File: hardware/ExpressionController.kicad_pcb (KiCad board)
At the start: 2 copper layers, 84.8 x 61.5 mm, 132 parts, among them J1 DC, J2 Exp1, J3 Exp2, J4 Exp3, J5 Exp4, Q1 DMP3099L-7, U1 ADP7142AUJZ-3.3, U10 74HC595, U11 SN74LVC126A, U12 74HC595, U13 SN74LVC126A, U14 74AHCT1G125, U2 ADP7142AUJZ-5.0, U3 ADP7142AUJZ-2.5, U4 AD7718, U5 AD7718, U6 74HC595, U7 SN74LVC126A, U8 74HC595, U9 SN74LVC126A, Y1 MS1V-T1K-32.768kHz-12.5pF-20P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, Y2 MS1V-T1K-32.768kHz-12.5pF-20P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

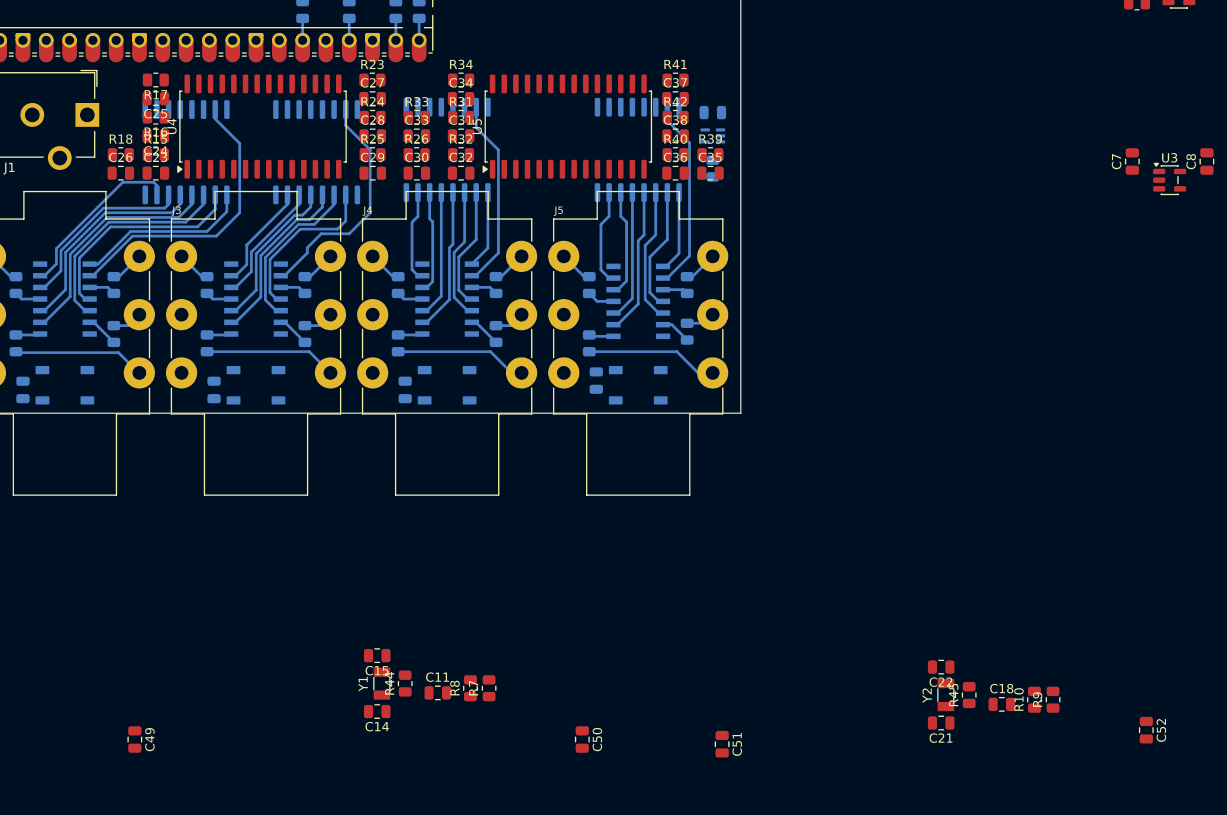
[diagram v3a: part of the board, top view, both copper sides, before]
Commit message: more routing changes
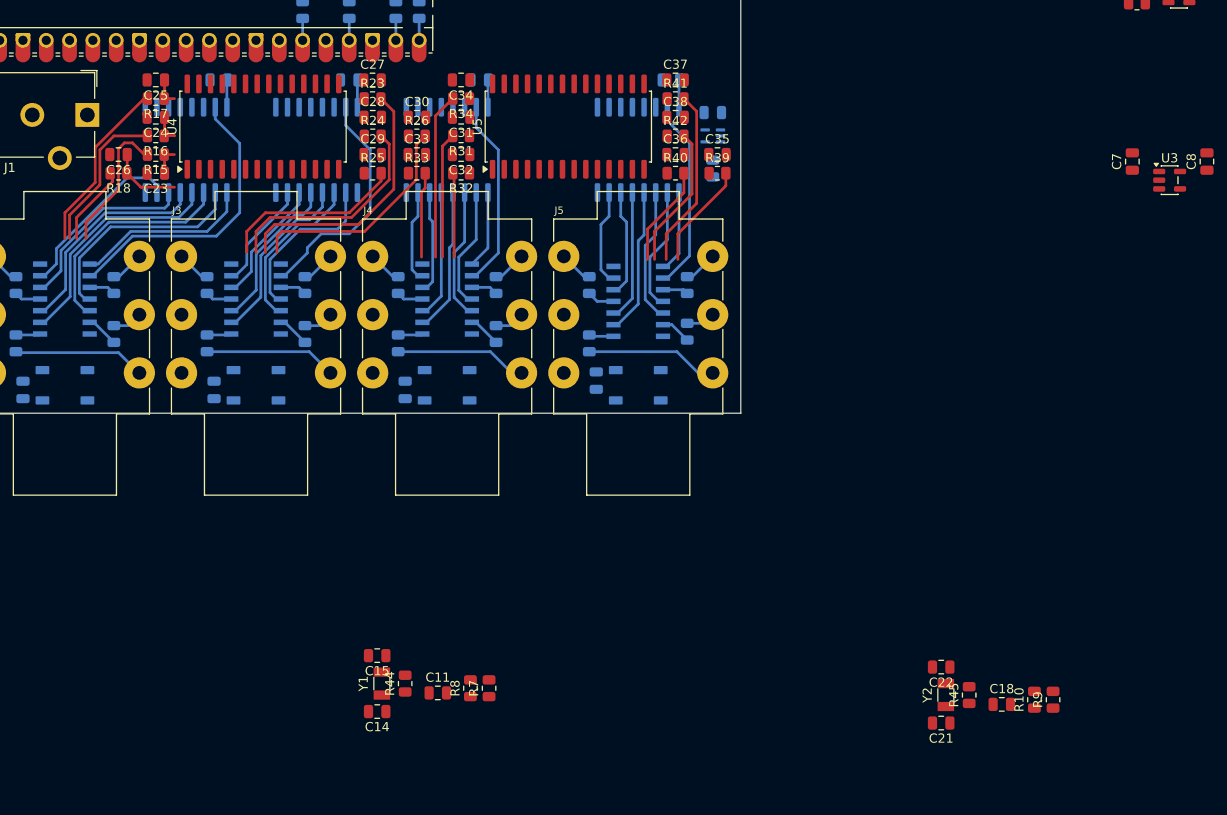
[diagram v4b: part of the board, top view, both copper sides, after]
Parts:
- C49, C50, C51, C52: moved to B.Cu
- moved C52 87.8 mm to (195.1, 148.1), turned to 180 degrees
- moved C51 77.1 mm to (174.2, 148.1), turned to 180 degrees
- moved C50 76.2 mm to (160.0, 148.1), turned to 180 degrees
- moved C49 72.5 mm to (145.8, 148.1), turned to 180 degrees
- moved C30 6.10 mm to (167.4, 152.1)
- moved R33 6.10 mm to (167.4, 158.2)
- moved C35 2.17 mm to (200.2, 156.2)
- moved R39 2.17 mm to (200.2, 158.2)
- moved C26 2.05 mm to (134.9, 156.2), turned to 180 degrees
- moved R18 2.05 mm to (134.9, 158.2), turned to 180 degrees
- moved R23 2.03 mm to (162.6, 150.1)
- moved R24 2.03 mm to (162.6, 154.2)
- moved R26 2.03 mm to (167.4, 154.2)
- moved R25 2.03 mm to (162.6, 158.2)
- moved C24 2.03 mm to (138.9, 152.1)
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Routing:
- net /AnalogFrontend/AnalogQuadChannel2/JACK1: track 3.70 -> 32.2 mm
- net /AnalogFrontend/AnalogQuadChannel2/JACK4: track 3.70 -> 28.4 mm
- net /AnalogFrontend/AnalogQuadChannel2/JACK2: track 3.28 -> 27.6 mm
- net /AnalogFrontend/AnalogQuadChannel2/JACK3: track 14.4 -> 34.5 mm
- net /AnalogFrontend/AnalogQuadChannel4/JACK3: track 14.4 -> 33.9 mm
- net /AnalogFrontend/AnalogQuadChannel1/JACK3: track 14.4 -> 33.6 mm
- net /AnalogFrontend/AnalogQuadChannel3/JACK4: track 3.70 -> 21.7 mm
- net /AnalogFrontend/AnalogQuadChannel1/JACK2: track 3.28 -> 20.1 mm
- net /AnalogFrontend/AnalogQuadChannel4/JACK4: track 3.70 -> 19.2 mm
- net /AnalogFrontend/AnalogQuadChannel1/JACK1: track 3.70 -> 18.9 mm
- net /AnalogFrontend/AnalogQuadChannel3/JACK1: track 3.70 -> 17.4 mm
- net +3.3V: track 0.00 -> 12.0 mm
- net /AnalogFrontend/AnalogQuadChannel4/JACK1: track 3.70 -> 15.3 mm
- net /AnalogFrontend/AnalogQuadChannel4/JACK2: track 3.17 -> 14.2 mm
- net /AnalogFrontend/AnalogQuadChannel3/JACK3: track 14.4 -> 23.7 mm
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
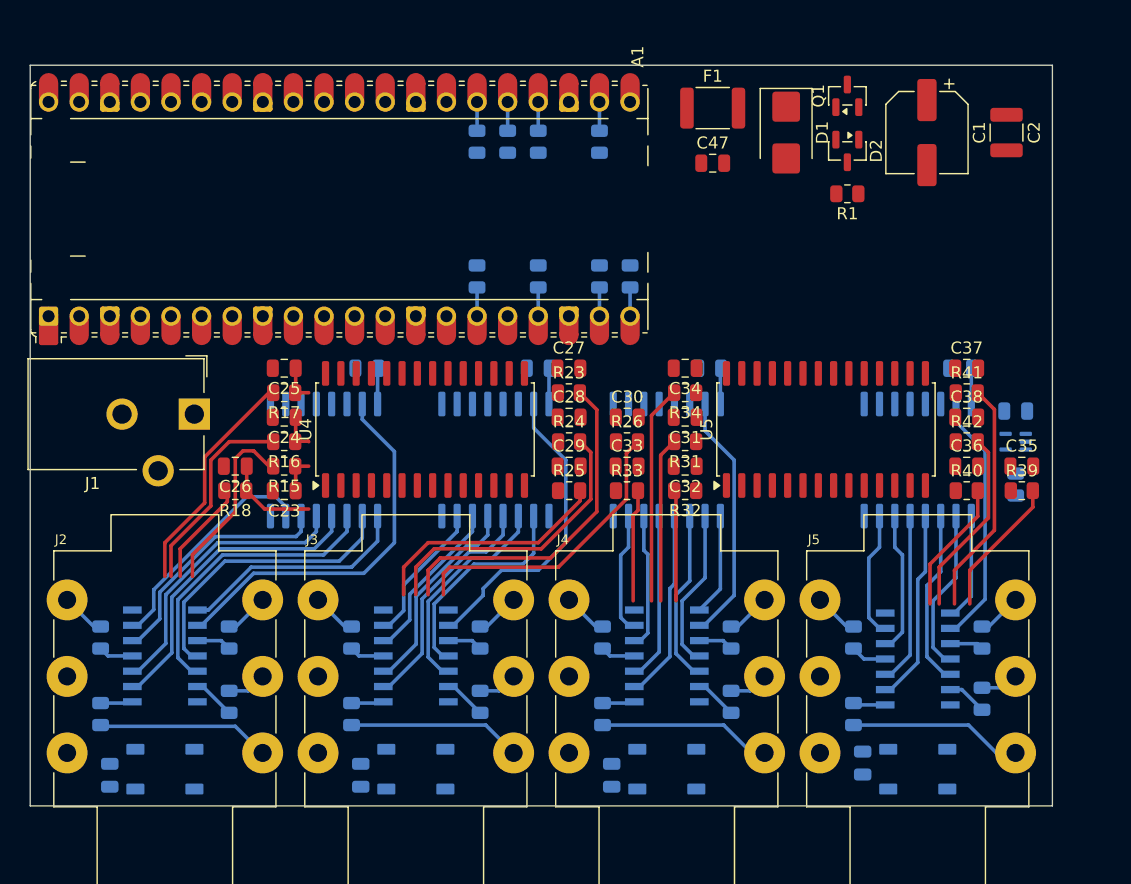
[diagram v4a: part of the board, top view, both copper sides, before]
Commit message: very tight layout
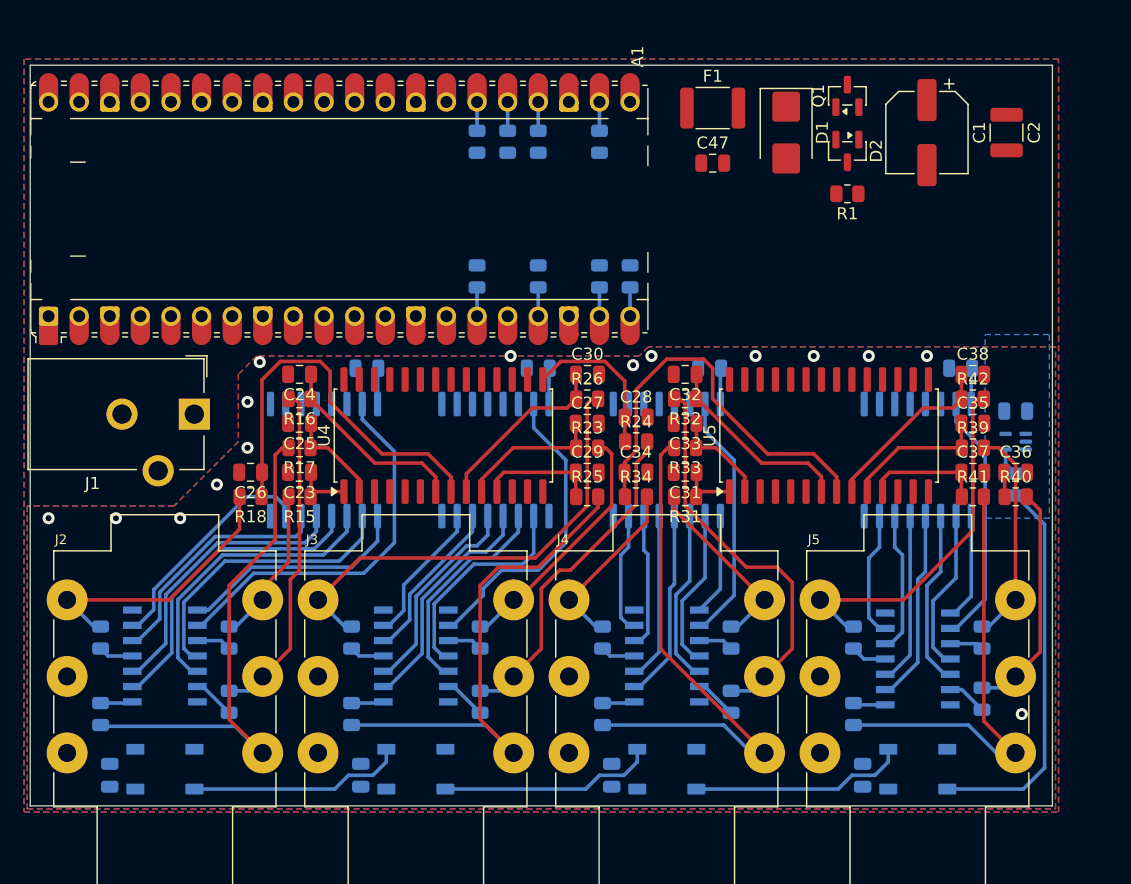
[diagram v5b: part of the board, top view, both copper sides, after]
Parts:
- moved C34 9.55 mm to (168.1, 156.7), turned to 0 degrees
- moved R34 9.55 mm to (168.1, 158.8), turned to 0 degrees
- moved C37 8.65 mm to (196.1, 156.7)
- moved R41 8.65 mm to (196.1, 158.8)
- moved C32 7.62 mm to (172.2, 148.6)
- moved R32 7.62 mm to (172.2, 150.6)
- moved C33 5.99 mm to (172.2, 152.7), turned to 180 degrees
- moved R33 5.99 mm to (172.2, 154.7), turned to 180 degrees
- moved C28 5.57 mm to (168.1, 152.1)
- moved R24 5.57 mm to (168.1, 154.2)
- moved C35 5.40 mm to (196.1, 152.7)
- moved R39 5.40 mm to (196.1, 154.7)
- moved C30 4.85 mm to (164.1, 148.6)
- moved R26 4.85 mm to (164.1, 150.6)
- moved C27 4.82 mm to (164.1, 152.7)
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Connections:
- U4 pad 10: /AnalogFrontend/AnalogQuadChannel2/ADC2 -> /AnalogFrontend/AnalogQuadChannel2/ADC1
- U4 pad 15: /AnalogFrontend/AnalogQuadChannel2/ADC4 -> /AnalogFrontend/AnalogQuadChannel2/ADC2
- U4 pad 2: /AnalogFrontend/AnalogQuadChannel1/ADC2 -> /AnalogFrontend/AnalogQuadChannel1/ADC3
- U4 pad 7: /AnalogFrontend/AnalogQuadChannel1/ADC3 -> /AnalogFrontend/AnalogQuadChannel1/ADC2
- U4 pad 9: /AnalogFrontend/AnalogQuadChannel2/ADC1 -> /AnalogFrontend/AnalogQuadChannel2/ADC4
- U5 pad 10: /AnalogFrontend/AnalogQuadChannel4/ADC2 -> /AnalogFrontend/AnalogQuadChannel4/ADC1
- U5 pad 15: /AnalogFrontend/AnalogQuadChannel4/ADC4 -> /AnalogFrontend/AnalogQuadChannel4/ADC2
- U5 pad 2: /AnalogFrontend/AnalogQuadChannel3/ADC2 -> /AnalogFrontend/AnalogQuadChannel3/ADC3
- U5 pad 7: /AnalogFrontend/AnalogQuadChannel3/ADC3 -> /AnalogFrontend/AnalogQuadChannel3/ADC2
- U5 pad 9: /AnalogFrontend/AnalogQuadChannel4/ADC1 -> /AnalogFrontend/AnalogQuadChannel4/ADC4
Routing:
- net /AnalogFrontend/AnalogQuadChannel3/ADC4: track 0.00 -> 33.8 mm
- net Net-(D4-DIN): track 0.00 -> 32.4 mm
- net /AnalogFrontend/AnalogQuadChannel1/ADC4: track 7.86 -> 32.7 mm
- net /AnalogFrontend/AnalogQuadChannel3/JACK2: track 12.5 -> 33.3 mm
- net /AnalogFrontend/AnalogQuadChannel3/JACK3: track 23.7 -> 44.3 mm
- net Net-(D4-DOUT): track 0.00 -> 17.9 mm
- net Net-(D6-DOUT): track 0.00 -> 17.9 mm
- net Net-(D5-DOUT): track 0.00 -> 17.9 mm
- net /AnalogFrontend/AnalogQuadChannel3/ADC2: track 0.00 -> 16.4 mm
- net /AnalogFrontend/AnalogQuadChannel2/ADC4: track 0.00 -> 15.2 mm
- net /AnalogFrontend/AnalogQuadChannel4/ADC4: track 0.00 -> 15.0 mm
- net /AnalogFrontend/AnalogQuadChannel1/ADC2: track 3.15 -> 16.3 mm
- net /AnalogFrontend/AnalogQuadChannel2/ADC2: track 0.00 -> 13.1 mm
- net /AnalogFrontend/AnalogQuadChannel2/ADC1: track 0.00 -> 12.0 mm
- net /AnalogFrontend/AnalogQuadChannel4/ADC1: track 0.00 -> 12.0 mm
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- added copper zone on B.Cu, net GND
- added copper zone on F.Cu, net GND
- added copper zone on B.Cu, net GNDA
- added copper zone on F.Cu, net GNDA

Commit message: schematic updates
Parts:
- removed JP1: 3V3 Select, Connector_PinHeader_2.54mm:PinHeader_1x03_P2.54mm_Vertical
- moved C49 92.5 mm to (229.4, 187.7)
- moved C50 92.5 mm to (243.6, 187.7)
- moved C51 92.5 mm to (257.8, 187.7)
- moved U10 92.5 mm to (254.3, 195.3)
- moved U12 92.5 mm to (275.1, 195.3)
- moved U6 92.5 mm to (225.8, 195.3)
- moved U8 92.5 mm to (240.0, 195.3)
- moved C52 92.5 mm to (278.6, 187.7)
- moved R29 79.6 mm to (92.7, 209.3)
- moved R30 79.6 mm to (92.7, 202.9)
- moved U9 79.6 mm to (77.2, 204.5)
- moved R11 79.6 mm to (61.7, 202.9)
- moved R12 79.6 mm to (61.7, 208.3)
- moved R21 79.6 mm to (71.9, 209.3)
- moved R22 79.6 mm to (71.9, 202.9)
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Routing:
- net /AnalogFrontend/AnalogQuadChannel3/JACK3: track 44.3 -> 0.00 mm
- net /AnalogFrontend/AnalogQuadChannel1/JACK3: track 43.2 -> 0.00 mm
- net /AnalogFrontend/AnalogQuadChannel2/JACK3: track 42.8 -> 0.00 mm
- net /AnalogFrontend/AnalogQuadChannel2/JACK4: track 38.8 -> 0.00 mm
- net /AnalogFrontend/AnalogQuadChannel4/JACK3: track 36.8 -> 0.00 mm
- net /AnalogFrontend/AnalogQuadChannel3/ADC4: track 33.8 -> 0.00 mm
- net /AnalogFrontend/AnalogQuadChannel3/JACK2: track 33.3 -> 0.00 mm
- net /AnalogFrontend/AnalogQuadChannel1/ADC4: track 32.7 -> 0.00 mm
- net Net-(D4-DIN): track 32.4 -> 0.00 mm
- net Net-(U6-QA): track 31.8 -> 0.00 mm
- net /AnalogFrontend/AnalogQuadChannel4/JACK4: track 30.4 -> 0.00 mm
- net /AnalogFrontend/AnalogQuadChannel1/JACK2: track 28.3 -> 0.00 mm
- net /AnalogFrontend/AnalogQuadChannel2/JACK2: track 27.9 -> 0.00 mm
- net Net-(U6-QE): track 25.9 -> 0.00 mm
- net Net-(U8-QA): track 25.5 -> 0.00 mm
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- removed copper zone on B.Cu, net GND
- removed copper zone on F.Cu, net GND
- removed copper zone on B.Cu, net GNDA
- removed copper zone on F.Cu, net GNDA
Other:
- board size 84.8 x 61.5 mm -> 87.6 x 72.6 mm

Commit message: replaced buffer ICs with analog switches, schematic bugfixes, started new routing
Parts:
- removed C7: 2.2u, Capacitor_SMD:C_0805_2012Metric
- removed NT1: NetTie_2, NetTie:NetTie-2_SMD_Pad2.0mm
- removed R11, R12, R13, R14, R19, R20, R21, R22, R27, R28, R29, R30, R35, R36, R37, R38: 1k, Resistor_SMD:R_0805_2012Metric
- removed R2: 8.2 1%, 1W, Resistor_SMD:R_0805_2012Metric
- removed U11, U13, U7, U9: SN74LVC126A, SN74LVC126A:SN74LVC126AD
- added C57: 100n, Capacitor_SMD:C_0805_2012Metric, F.Cu at (279.2, 132.1)
- added C58: 100n, Capacitor_SMD:C_0805_2012Metric, F.Cu at (294.4, 132.1)
- added C59: 100n, Capacitor_SMD:C_0805_2012Metric, F.Cu at (294.4, 147.6)
- added C60: 100n, Capacitor_SMD:C_0805_2012Metric, F.Cu at (279.2, 147.6)
- added R50: 1k, Resistor_SMD:R_0805_2012Metric, B.Cu at (114.0, 179.6)
- added R51: 1k, Resistor_SMD:R_0805_2012Metric, F.Cu at (294.4, 126.2)
- added R52: 1k, Resistor_SMD:R_0805_2012Metric, F.Cu at (294.4, 141.6)
- added R53: 1k, Resistor_SMD:R_0805_2012Metric, F.Cu at (279.2, 141.6)
- added R54: 1k, Resistor_SMD:R_0805_2012Metric, F.Cu at (110.7, 184.2)
- added R55: 1k, Resistor_SMD:R_0805_2012Metric, F.Cu at (294.4, 129.1)
- added R56: 1k, Resistor_SMD:R_0805_2012Metric, F.Cu at (294.4, 144.6)
- added R57: 1k, Resistor_SMD:R_0805_2012Metric, F.Cu at (279.2, 144.6)
- added R58: 10k, Resistor_SMD:R_0805_2012Metric, F.Cu at (273.1, 113.3)
- added R59: 47, Resistor_SMD:R_0805_2012Metric, F.Cu at (260.4, 112.3)
- added U15: TMUX1511PWR, Package_SO:TSSOP-14_4.4x5mm_P0.65mm, B.Cu at (123.4, 171.7)
- added U16: TMUX1511PWR, Package_SO:TSSOP-14_4.4x5mm_P0.65mm, F.Cu at (287.8, 128.2)
- added U17: TMUX1511PWR, Package_SO:TSSOP-14_4.4x5mm_P0.65mm, F.Cu at (287.8, 143.6)
- added U18: TMUX1511PWR, Package_SO:TSSOP-14_4.4x5mm_P0.65mm, F.Cu at (272.6, 143.6)
- added U19: TMUX1511PWR, Package_SO:TSSOP-14_4.4x5mm_P0.65mm, B.Cu at (133.1, 171.7)
- added U20: TMUX1511PWR, Package_SO:TSSOP-14_4.4x5mm_P0.65mm, F.Cu at (287.8, 134.9)
- added U21: TMUX1511PWR, Package_SO:TSSOP-14_4.4x5mm_P0.65mm, F.Cu at (287.8, 150.3)
- added U22: TMUX1511PWR, Package_SO:TSSOP-14_4.4x5mm_P0.65mm, F.Cu at (272.6, 150.3)
- C14, C15, C21, C22: value 15p -> 18p
- C2: footprint Capacitor_SMD:C_1210_3225Metric -> Capacitor_SMD:C_0805_2012Metric
- C23, C24, C25, C26, C27, C28, C29, C30, C31, C32, C33, C34, C35, C36, C37, C38: value 100n -> 10n
- C3, C5: value 2.2u -> 4.7u
- R10, R3, R4, R46, R47, R48, R49, R5, R6, R7, R8, R9: value 22 -> 47
- R15, R16, R17, R18, R23, R24, R25, R26, R31, R32, R33, R34, R39, R40, R41, R42: value 1k -> 10k
- moved U6 98.4 mm to (128.3, 182.1), turned to -90 degrees
- moved R16 81.1 mm to (125.5, 166.4), turned to -90 degrees
- moved R17 79.8 mm to (122.9, 166.4), turned to -90 degrees
- moved C24 79.5 mm to (125.5, 162.3), turned to 90 degrees
- moved C25 78.3 mm to (122.9, 162.3), turned to 90 degrees
- moved R18 75.8 mm to (120.4, 166.4), turned to -90 degrees
- moved C26 74.4 mm to (120.4, 162.3), turned to 90 degrees
- moved R15 73.3 mm to (128.0, 166.4), turned to -90 degrees
- moved C23 71.9 mm to (128.0, 162.3), turned to 90 degrees
- moved U5 67.3 mm to (181.6, 161.5)
- moved C39 0.76 mm to (187.7, 191.8), turned to -90 degrees
- moved D4 0.76 mm to (192.3, 191.3)
- moved J5 0.76 mm to (200.4, 177.2)
- moved J4 0.51 mm to (179.1, 177.2)
- moved C40 0.51 mm to (166.4, 191.8), turned to -90 degrees
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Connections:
- A1 pad 16: unconnected-(A1-GPIO12-Pad16) -> SR_WB
- A1 pad 36: 3V3_PICO -> unconnected-(A1-3V3-Pad36)_1
- C10 pad 1: VDDA -> +3.3VA
- C10 pad 2: GNDA -> GND
- C11 pad 1: +3.3V -> +3.3VA
- C13 pad 1: VDDA -> +2.5V
- C13 pad 2: GNDA -> GND
- C16 pad 1: VDDA -> +3.3VA
- C16 pad 2: GNDA -> GND
- C17 pad 1: VDDA -> +3.3VA
- C17 pad 2: GNDA -> GND
- C18 pad 1: +3.3V -> +3.3VA
- C20 pad 1: VDDA -> +2.5V
- C20 pad 2: GNDA -> GND
- C23 pad 2: GNDA -> GND
- C24 pad 2: GNDA -> GND
- C25 pad 2: GNDA -> GND
- C26 pad 2: GNDA -> GND
- C27 pad 2: GNDA -> GND
- C28 pad 2: GNDA -> GND
- C29 pad 2: GNDA -> GND
- C30 pad 2: GNDA -> GND
- C31 pad 2: GNDA -> GND
- C32 pad 2: GNDA -> GND
- C33 pad 2: GNDA -> GND
- C34 pad 2: GNDA -> GND
- C35 pad 2: GNDA -> GND
- C36 pad 2: GNDA -> GND
- C37 pad 2: GNDA -> GND
- C38 pad 2: GNDA -> GND
- C4 pad 1: Net-(JP1-B) -> +3.3VA
- C49 pad 1: +3.3V -> +3.3VA
- C5 pad 1: Net-(U2-EN) -> VEXT
- C50 pad 1: +3.3V -> +3.3VA
- C51 pad 1: +3.3V -> +3.3VA
- C52 pad 1: +3.3V -> +3.3VA
- C53 pad 1: VDDA -> +3.3VA
- C53 pad 2: GNDA -> GND
- C54 pad 1: VDDA -> +3.3VA
- C54 pad 2: GNDA -> GND
- C55 pad 1: VDDA -> +3.3VA
- C55 pad 2: GNDA -> GND
- C56 pad 1: VDDA -> +3.3VA
- C56 pad 2: GNDA -> GND
- C8 pad 1: VDDA -> +2.5V
- C8 pad 2: GNDA -> GND
- C9 pad 1: VDDA -> +3.3VA
- C9 pad 2: GNDA -> GND
- D2 pad 1: VEXT -> Net-(D2-A)
- D2 pad 3: Net-(D2-K) -> VEXT
- Q1 pad 1: Net-(D2-K) -> Net-(D2-A)
- R1 pad 1: Net-(D2-K) -> Net-(D2-A)
- U1 pad 4: Net-(JP1-B) -> +3.3VA
- U1 pad 5: Net-(JP1-B) -> +3.3VA
- U10 pad 10: +3.3V -> +3.3VA
- U10 pad 16: +3.3V -> +3.3VA
- U12 pad 10: +3.3V -> +3.3VA
- U12 pad 16: +3.3V -> +3.3VA
- U2 pad 1: Net-(U2-EN) -> VEXT
- U2 pad 3: Net-(U2-EN) -> VEXT
- U3 pad 1: VEXT -> +3.3VA
- U3 pad 2: GNDA -> GND
- U3 pad 3: VEXT -> +3.3VA
- U3 pad 4: VDDA -> +2.5V
- U3 pad 5: VDDA -> +2.5V
- U4 pad 1: /AnalogFrontend/AnalogQuadChannel1/ADC1 -> /AnalogFrontend/AnalogQuadChannel2/ADC3
- U4 pad 10: /AnalogFrontend/AnalogQuadChannel2/ADC1 -> /AnalogFrontend/AnalogQuadChannel1/ADC4
- U4 pad 11: /AnalogFrontend/AnalogQuadChannel2/ADC3 -> /AnalogFrontend/AnalogQuadChannel2/ADC1
- U4 pad 12: GNDA -> GND
- U4 pad 13: unconnected-(U4-REFIN2(+)/AIN9-Pad13) -> /AnalogFrontend/AnalogQuadChannel2/ADC2
- U4 pad 14: unconnected-(U4-REFIN2(-)/AIN10-Pad14) -> +2.5V
- U4 pad 15: /AnalogFrontend/AnalogQuadChannel2/ADC2 -> GND
- U4 pad 17: GNDA -> GND
- U4 pad 19: +3.3V -> +3.3VA
- U4 pad 2: /AnalogFrontend/AnalogQuadChannel1/ADC3 -> /AnalogFrontend/AnalogQuadChannel2/ADC4
- U4 pad 26: +3.3V -> +3.3VA
- U4 pad 3: VDDA -> +3.3VA
- U4 pad 4: GNDA -> GND
- U4 pad 5: GNDA -> GND
- U4 pad 6: VDDA -> +2.5V
- U4 pad 7: /AnalogFrontend/AnalogQuadChannel1/ADC2 -> /AnalogFrontend/AnalogQuadChannel1/ADC1
- U4 pad 8: /AnalogFrontend/AnalogQuadChannel1/ADC4 -> /AnalogFrontend/AnalogQuadChannel1/ADC2
- U4 pad 9: /AnalogFrontend/AnalogQuadChannel2/ADC4 -> /AnalogFrontend/AnalogQuadChannel1/ADC3
- U5 pad 1: /AnalogFrontend/AnalogQuadChannel3/ADC1 -> /AnalogFrontend/AnalogQuadChannel4/ADC3
- U5 pad 10: /AnalogFrontend/AnalogQuadChannel4/ADC1 -> /AnalogFrontend/AnalogQuadChannel3/ADC4
- U5 pad 11: /AnalogFrontend/AnalogQuadChannel4/ADC3 -> /AnalogFrontend/AnalogQuadChannel4/ADC1
- U5 pad 12: GNDA -> GND
- U5 pad 13: unconnected-(U5-REFIN2(+)/AIN9-Pad13) -> /AnalogFrontend/AnalogQuadChannel4/ADC2
- U5 pad 14: unconnected-(U5-REFIN2(-)/AIN10-Pad14) -> +2.5V
- U5 pad 15: /AnalogFrontend/AnalogQuadChannel4/ADC2 -> GND
- U5 pad 17: GNDA -> GND
- U5 pad 19: +3.3V -> +3.3VA
- U5 pad 2: /AnalogFrontend/AnalogQuadChannel3/ADC3 -> /AnalogFrontend/AnalogQuadChannel4/ADC4
- U5 pad 26: +3.3V -> +3.3VA
- U5 pad 3: VDDA -> +3.3VA
- U5 pad 4: GNDA -> GND
- U5 pad 5: GNDA -> GND
- U5 pad 6: VDDA -> +2.5V
- U5 pad 7: /AnalogFrontend/AnalogQuadChannel3/ADC2 -> /AnalogFrontend/AnalogQuadChannel3/ADC1
- U5 pad 8: /AnalogFrontend/AnalogQuadChannel3/ADC4 -> /AnalogFrontend/AnalogQuadChannel3/ADC2
- U5 pad 9: /AnalogFrontend/AnalogQuadChannel4/ADC4 -> /AnalogFrontend/AnalogQuadChannel3/ADC3
- U6 pad 10: +3.3V -> +3.3VA
- U6 pad 16: +3.3V -> +3.3VA
- U8 pad 10: +3.3V -> +3.3VA
- U8 pad 16: +3.3V -> +3.3VA
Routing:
- net /AnalogFrontend/AnalogQuadChannel1/JACK3: track 0.00 -> 40.6 mm, vias 0 -> 2
- net /AnalogFrontend/AnalogQuadChannel1/JACK2: track 0.00 -> 35.4 mm, vias 0 -> 1
- net /AnalogFrontend/AnalogQuadChannel1/JACK4: track 0.00 -> 29.8 mm, vias 0 -> 1
- net /AnalogFrontend/AnalogQuadChannel1/JACK1: track 0.00 -> 24.8 mm, vias 0 -> 1
- net Net-(U15-SEL3): track 0.00 -> 16.9 mm
- net Net-(U15-SEL1): track 0.00 -> 10.1 mm
- net Net-(U15-SEL4): track 0.00 -> 8.86 mm
- net Net-(U15-SEL2): track 0.00 -> 8.31 mm
- net /AnalogFrontend/AnalogQuadChannel1/ADC4: track 0.00 -> 2.20 mm
- net /AnalogFrontend/AnalogQuadChannel1/ADC3: track 0.00 -> 2.20 mm
- net /AnalogFrontend/AnalogQuadChannel1/ADC2: track 0.00 -> 2.20 mm
- net /AnalogFrontend/AnalogQuadChannel1/ADC1: track 0.00 -> 2.20 mm
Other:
- board size 87.6 x 72.6 mm -> 86.6 x 72.6 mm
